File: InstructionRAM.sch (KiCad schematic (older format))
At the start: 6 parts, among them U18 IDT7008L15JG, U19 ATF22V10C-7PX, U20 IDT7008L15JG

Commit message: Use IDT 7024L15PFG dual port SRAM for the register file.
These are smaller and faster than the ICs I was using before, and I only
need two of them.
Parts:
- renumbered C23 to C69, C24 to C70, C25 to C71, U18 to U65, U19 to U66, U20 to U67

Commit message: Fix ERC errors and change operands in EX.
Now, A is the left operand and B is the right operand. The immediate
value may be selected for the right hand operand.
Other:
- note removed: "TODO: Consider replacing these two dual port SRAMs\nwith one 7028L20PFGI 64Kx16 dual port SRAM."
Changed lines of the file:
@@
 Wire Bus Line
 	6400 950  8650 950
-Text Notes 4300 1900 0    50   ~ 0
-TODO: Consider replacing these two dual port SRAMs\nwith one 7028L20PFGI 64Kx16 dual port SRAM.
 $Comp
 L power:GND #PWR?

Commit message: Add a "Mouser" field to components with a link to buy the part.
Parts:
- C68: renamed from C69; Mouser (none) -> https://www.mouser.com/ProductDetail/963-EMK107B7104KAHT
- C69: renamed from C70; Mouser (none) -> https://www.mouser.com/ProductDetail/963-EMK107B7104KAHT
- C70: renamed from C71; Mouser (none) -> https://www.mouser.com/ProductDetail/963-EMK107B7104KAHT
- U64: renamed from U65; Mouser (none) -> https://www.mouser.com/ProductDetail/Renesas-IDT/7008L15JG?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; Mouser2 (none) -> https://www.mouser.com/ProductDetail/3M-Electronic-Solution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
- U65: renamed from U66; Mouser (none) -> https://www.mouser.com/ProductDetail/Microchip-Technology-A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; Mouser2 (none) -> https://www.mouser.com/ProductDetail/575-4462401
- U66: renamed from U67; Mouser (none) -> https://www.mouser.com/ProductDetail/Renesas-IDT/7008L15JG?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; Mouser2 (none) -> https://www.mouser.com/ProductDetail/3M-Electronic-Solution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
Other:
- note added: "TODO: The ATF22V10 data sheet suggests connecting pin 15"

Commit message: The right operand can form an immediate value from several bit fields.
This solves the problem of the Store instruction not being able to compute
Ra+Imm as can be done in the Load instruction. Now, it can get those
immediate bits from the unused 'c' field.

Also, Jump isntructions which do not use the 'c' field to specify a link
register can use those bits to form an eight-bit immediate value.
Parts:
- renumbered C68 to C72, C69 to C73, C70 to C74, U64 to U68, U65 to U69, U66 to U70

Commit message: The Store Operand can take a byte-swapped value from the B register.
This enabled a version of the Store instruction which writes the upper
byte of the register to memory.
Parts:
- renumbered C72 to C74, C73 to C75, C74 to C76, U68 to U70, U69 to U71, U70 to U72

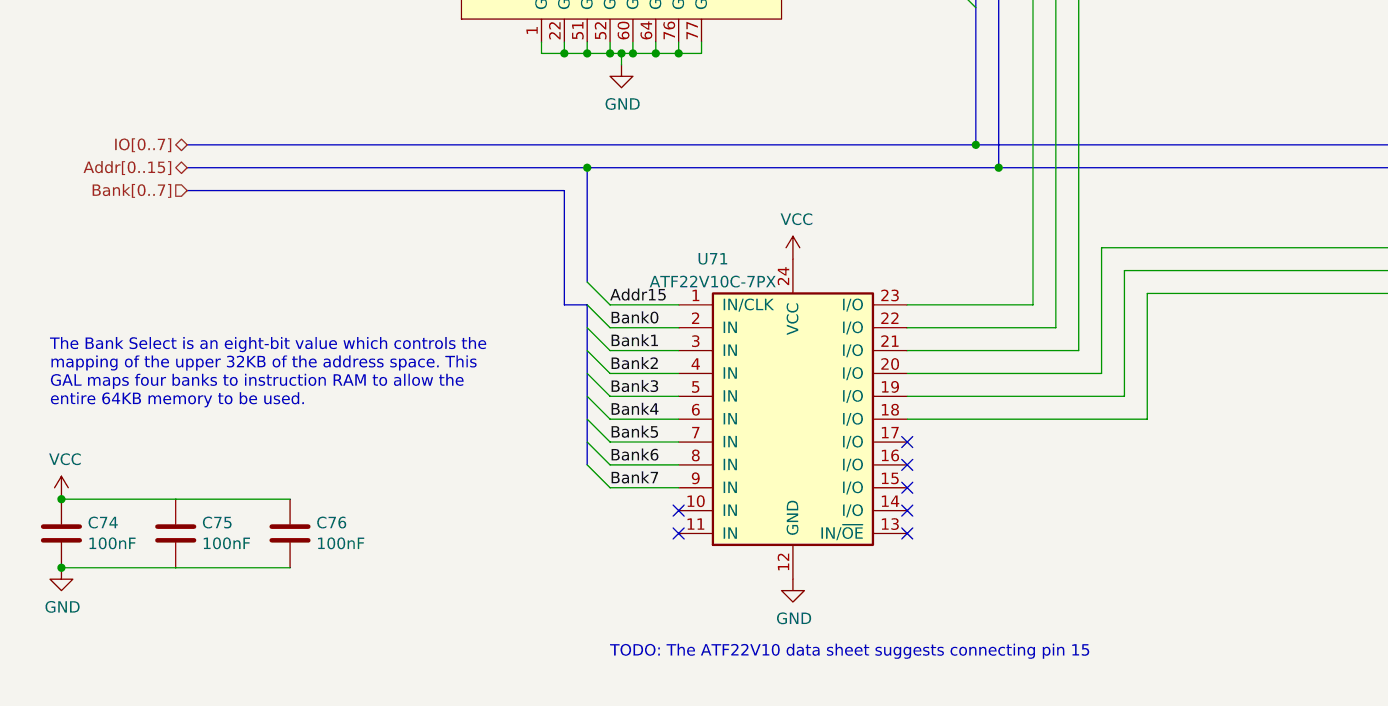
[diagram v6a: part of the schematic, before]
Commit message: Instruction RAM must accept MemLoad, MemStore, and Phi2 signals.
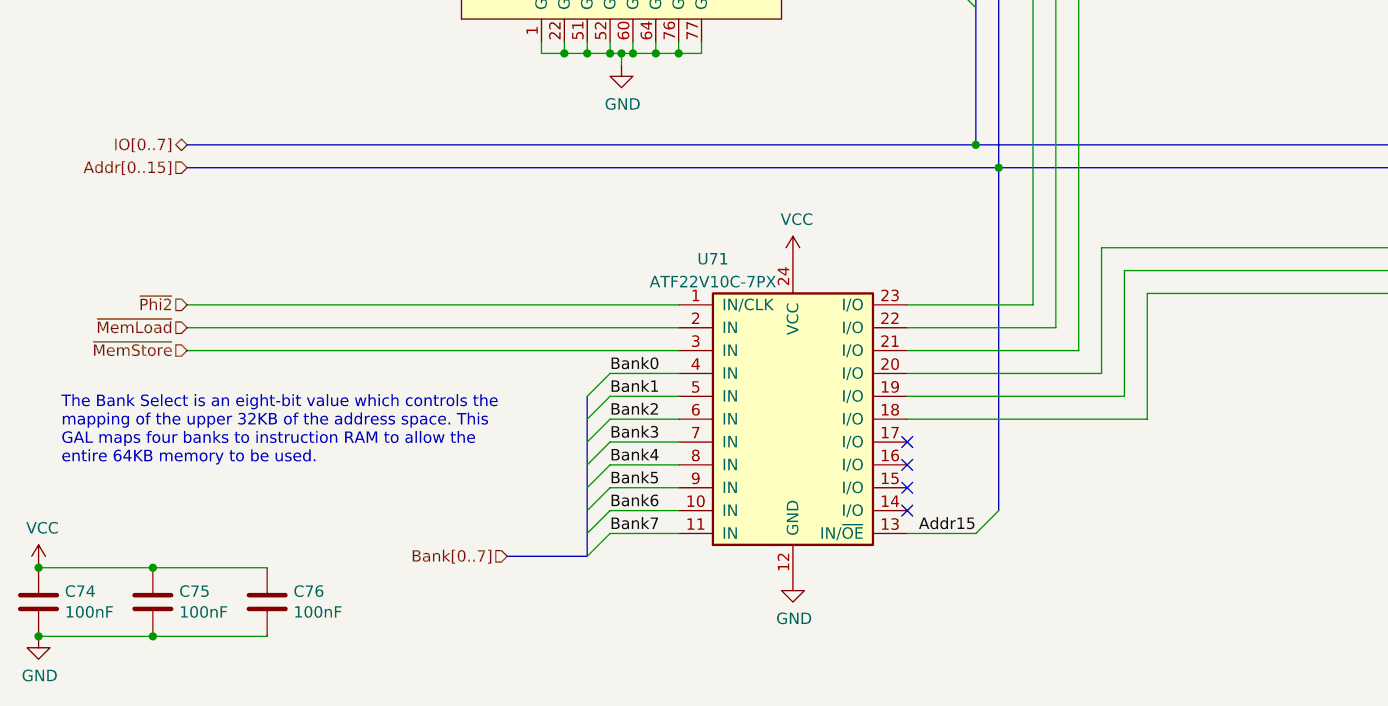
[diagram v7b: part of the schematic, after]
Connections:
- net Addr15: now also U71.13 (IN/~OE); no longer U71.1 (IN/CLK)
- net Bank0: now also U71.4 (IN); no longer U71.2 (IN)
- net Bank1: now also U71.5 (IN); no longer U71.3 (IN)
- net Bank2: now also U71.6 (IN); no longer U71.4 (IN)
- net Bank3: now also U71.7 (IN); no longer U71.5 (IN)
- net Bank4: now also U71.8 (IN); no longer U71.6 (IN)
- net Bank5: now also U71.9 (IN); no longer U71.7 (IN)
- net Bank6: now also U71.10 (IN); no longer U71.8 (IN)
- net Bank7: now also U71.11 (IN); no longer U71.9 (IN)
- new net ~MemLoad: U71.2 (IN)
- new net ~MemStore: U71.3 (IN)
- new net ~Phi2: U71.1 (IN/CLK)
- no-connect marks 11 -> 8
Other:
- note removed: "TODO: The ATF22V10 data sheet suggests connecting pin 15"
- moved on the sheet: C74, C75, C76
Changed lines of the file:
@@
 L Device:C C?
 U 1 1 5FD4710E
-P 700 7350
+P 600 7650
 AR Path="/5D8005AF/5D800742/5FD4710E" Ref="C?"  Part="1"
 AR Path="/5FE35007/5FD4710E" Ref="C?"  Part="1"
 AR Path="/5FE35007/5FD0D8DC/5FD4710E" Ref="C74"  Part="1"
-F 0 "C74" H 815 7396 50  0000 L CNN
-F 1 "100nF" H 815 7305 50  0000 L CNN
-F 2 "Capacitor_SMD:C_0603_1608Metric_Pad1.08x0.95mm_HandSolder" H 738 7200 50  0001 C CNN
-F 3 "~" H 700 7350 50  0001 C CNN
-F 4 "https://www.mouser.com/ProductDetail/963-EMK107B7104KAHT" H 700 7350 50  0001 C CNN "Mouser"
-	1    700  7350
+F 0 "C74" H 715 7696 50  0000 L CNN
+F 1 "100nF" H 715 7605 50  0000 L CNN
+F 2 "Capacitor_SMD:C_0603_1608Metric_Pad1.08x0.95mm_HandSolder" H 638 7500 50  0001 C CNN
+F 3 "~" H 600 7650 50  0001 C CNN
+F 4 "https://www.mouser.com/ProductDetail/963-EMK107B7104KAHT" H 600 7650 50  0001 C CNN "Mouser"
+	1    600  7650
 	1    0    0    -1
 $EndComp
@@
 L Device:C C?
 U 1 1 5FD47114
-P 1200 7350
+P 1100 7650
 AR Path="/5D8005AF/5D800742/5FD47114" Ref="C?"  Part="1"
 AR Path="/5FE35007/5FD47114" Ref="C?"  Part="1"
 AR Path="/5FE35007/5FD0D8DC/5FD47114" Ref="C75"  Part="1"
-F 0 "C75" H 1315 7396 50  0000 L CNN
-F 1 "100nF" H 1315 7305 50  0000 L CNN
-F 2 "Capacitor_SMD:C_0603_1608Metric_Pad1.08x0.95mm_HandSolder" H 1238 7200 50  0001 C CNN
-F 3 "~" H 1200 7350 50  0001 C CNN
-F 4 "https://www.mouser.com/ProductDetail/963-EMK107B7104KAHT" H 1200 7350 50  0001 C CNN "Mouser"
-	1    1200 7350
+F 0 "C75" H 1215 7696 50  0000 L CNN
+F 1 "100nF" H 1215 7605 50  0000 L CNN
+F 2 "Capacitor_SMD:C_0603_1608Metric_Pad1.08x0.95mm_HandSolder" H 1138 7500 50  0001 C CNN
+F 3 "~" H 1100 7650 50  0001 C CNN
+F 4 "https://www.mouser.com/ProductDetail/963-EMK107B7104KAHT" H 1100 7650 50  0001 C CNN "Mouser"
+	1    1100 7650
 	1    0    0    -1
 $EndComp
@@
 L power:GND #PWR?
 U 1 1 5FD4711A
-P 700 7500
+P 600 7800
 AR Path="/5D8005AF/5D800742/5FD4711A" Ref="#PWR?"  Part="1"
 AR Path="/5FE35007/5FD4711A" Ref="#PWR?"  Part="1"
 AR Path="/5FE35007/5FD0D8DC/5FD4711A" Ref="#PWR0450"  Part="1"
-F 0 "#PWR0450" H 700 7250 50  0001 C CNN
-F 1 "GND" H 705 7327 50  0000 C CNN
-F 2 "" H 700 7500 50  0001 C CNN
-F 3 "" H 700 7500 50  0001 C CNN
-	1    700  7500
+F 0 "#PWR0450" H 600 7550 50  0001 C CNN
+F 1 "GND" H 605 7627 50  0000 C CNN
+F 2 "" H 600 7800 50  0001 C CNN
+F 3 "" H 600 7800 50  0001 C CNN
+	1    600  7800
 	1    0    0    -1
 $EndComp
@@
 L power:VCC #PWR?
 U 1 1 5FD47120
-P 700 7200
+P 600 7500
 AR Path="/5D8005AF/5D800742/5FD47120" Ref="#PWR?"  Part="1"
 AR Path="/5FE35007/5FD47120" Ref="#PWR?"  Part="1"
 AR Path="/5FE35007/5FD0D8DC/5FD47120" Ref="#PWR0449"  Part="1"
-F 0 "#PWR0449" H 700 7050 50  0001 C CNN
-F 1 "VCC" H 717 7373 50  0000 C CNN
-F 2 "" H 700 7200 50  0001 C CNN
-F 3 "" H 700 7200 50  0001 C CNN
-	1    700  7200
+F 0 "#PWR0449" H 600 7350 50  0001 C CNN
+F 1 "VCC" H 617 7673 50  0000 C CNN
+F 2 "" H 600 7500 50  0001 C CNN
+F 3 "" H 600 7500 50  0001 C CNN
+	1    600  7500
 	1    0    0    -1
 $EndComp
 Wire Wire Line
-	700  7200 1200 7200
-Connection ~ 700  7200
-Wire Wire Line
-	1200 7500 700  7500
-Connection ~ 700  7500
+	600  7500 1100 7500
+Connection ~ 600  7500
+Wire Wire Line
+	1100 7800 600  7800
+Connection ~ 600  7800
 Entry Wire Line
 	6500 4250 6400 4150
@@
 L Device:C C?
 U 1 1 5FD472D1
-P 1700 7350
+P 1600 7650
 AR Path="/5D8005AF/5D800742/5FD472D1" Ref="C?"  Part="1"
 AR Path="/5FE35007/5FD472D1" Ref="C?"  Part="1"
 AR Path="/5FE35007/5FD0D8DC/5FD472D1" Ref="C76"  Part="1"
-F 0 "C76" H 1815 7396 50  0000 L CNN
-F 1 "100nF" H 1815 7305 50  0000 L CNN
-F 2 "Capacitor_SMD:C_0603_1608Metric_Pad1.08x0.95mm_HandSolder" H 1738 7200 50  0001 C CNN
-F 3 "~" H 1700 7350 50  0001 C CNN
-F 4 "https://www.mouser.com/ProductDetail/963-EMK107B7104KAHT" H 1700 7350 50  0001 C CNN "Mouser"
-	1    1700 7350
+F 0 "C76" H 1715 7696 50  0000 L CNN
+F 1 "100nF" H 1715 7605 50  0000 L CNN
+F 2 "Capacitor_SMD:C_0603_1608Metric_Pad1.08x0.95mm_HandSolder" H 1638 7500 50  0001 C CNN
+F 3 "~" H 1600 7650 50  0001 C CNN
+F 4 "https://www.mouser.com/ProductDetail/963-EMK107B7104KAHT" H 1600 7650 50  0001 C CNN "Mouser"
+	1    1600 7650
 	1    0    0    -1
 $EndComp
 Wire Wire Line
-	1200 7200 1700 7200
-Wire Wire Line
-	1700 7500 1200 7500
+	1100 7500 1600 7500
+Wire Wire Line
+	1600 7800 1100 7800
 Text HLabel 1250 5650 0    50   3State ~ 0
 IO[0..7]
-Text HLabel 1250 5750 0    50   3State ~ 0
+Text HLabel 1250 5750 0    50   Input ~ 0
 Addr[0..15]
 Wire Bus Line
@@
 Wire Wire Line
 	10150 2250 8950 2250
-Entry Wire Line
-	3000 6250 3100 6350
-Wire Wire Line
-	3100 6350 3400 6350
-Text Label 3100 6350 0    50   ~ 0
-Addr15
-Text HLabel 1250 5850 0    50   Input ~ 0
+Text HLabel 2650 7450 0    50   Input ~ 0
 Bank[0..7]
-Entry Wire Line
-	3000 6350 3100 6450
-Text Label 3100 6450 0    50   ~ 0
+Text Label 3100 6650 0    50   ~ 0
 Bank0
 Entry Wire Line
-	3000 6450 3100 6550
-Text Label 3100 6550 0    50   ~ 0
+	3100 6750 3000 6850
+Text Label 3100 6750 0    50   ~ 0
 Bank1
 Entry Wire Line
-	3000 6550 3100 6650
-Text Label 3100 6650 0    50   ~ 0
+	3100 6850 3000 6950
+Text Label 3100 6850 0    50   ~ 0
 Bank2
-Wire Bus Line
-	1250 5850 2900 5850
 Text Label 9700 3950 2    50   ~ 0
 Addr14
@@
 Entry Wire Line
 	4700 2550 4800 2650
-Text Notes 650  6800 0    50   ~ 0
+Text Notes 700  7050 0    50   ~ 0
 The Bank Select is an eight-bit value which controls the\nmapping of the upper 32KB of the address space. This\nGAL maps four banks to instruction RAM to allow the\nentire 64KB memory to be used.
-Wire Bus Line
-	1250 5750 3000 5750
-Connection ~ 3000 5750
-Wire Bus Line
-	3000 5750 4800 5750
 Wire Bus Line
 	4800 5750 9800 5750
 NoConn ~ 4400 6950
 NoConn ~ 4400 7050
-NoConn ~ 4400 7150
 NoConn ~ 4400 7250
-NoConn ~ 4400 7350
-NoConn ~ 3400 7250
-NoConn ~ 3400 7350
-Wire Bus Line
-	3000 5750 3000 6250
-Wire Wire Line
-	3100 6450 3400 6450
-Wire Wire Line
-	3100 6550 3400 6550
 Wire Wire Line
 	3100 6650 3400 6650
-Wire Bus Line
-	3000 6350 2900 6350
-Wire Bus Line
-	2900 6350 2900 5850
+Wire Wire Line
+	3100 6750 3400 6750
+Wire Wire Line
+	3100 6850 3400 6850
 $Comp
 L MainBoard-rescue:ATF22V10C-Logic_Programmable U?
@@
 $EndComp
 Entry Wire Line
-	3000 6650 3100 6750
-Text Label 3100 6750 0    50   ~ 0
+	3100 6950 3000 7050
+Text Label 3100 6950 0    50   ~ 0
 Bank3
 Entry Wire Line
-	3000 6750 3100 6850
-Text Label 3100 6850 0    50   ~ 0
+	3100 7050 3000 7150
+Text Label 3100 7050 0    50   ~ 0
 Bank4
 Entry Wire Line
-	3000 6850 3100 6950
-Text Label 3100 6950 0    50   ~ 0
+	3100 7150 3000 7250
+Text Label 3100 7150 0    50   ~ 0
 Bank5
 Wire Wire Line
-	3100 6750 3400 6750
-Wire Wire Line
-	3100 6850 3400 6850
-Wire Wire Line
 	3100 6950 3400 6950
-Entry Wire Line
-	3000 6950 3100 7050
-Text Label 3100 7050 0    50   ~ 0
+Wire Wire Line
+	3100 7050 3400 7050
+Wire Wire Line
+	3100 7150 3400 7150
+Entry Wire Line
+	3100 7250 3000 7350
+Text Label 3100 7250 0    50   ~ 0
 Bank6
 Entry Wire Line
-	3000 7050 3100 7150
-Text Label 3100 7150 0    50   ~ 0
+	3100 7350 3000 7450
+Text Label 3100 7350 0    50   ~ 0
 Bank7
 Wire Wire Line
-	3100 7050 3400 7050
-Wire Wire Line
-	3100 7150 3400 7150
+	3100 7250 3400 7250
+Wire Wire Line
+	3100 7350 3400 7350
 Wire Wire Line
 	4950 6350 4400 6350
@@
 NoConn ~ 2350 1850
 NoConn ~ 3950 1850
-Wire Bus Line
-	3000 6350 3000 7050
+Text HLabel 1250 6450 0    50   Input ~ 0
+~MemLoad
+Text HLabel 1250 6550 0    50   Input ~ 0
+~MemStore
+Text HLabel 1250 6350 0    50   Input ~ 0
+~Phi2
+Connection ~ 1100 7500
+Connection ~ 1100 7800
+Entry Wire Line
+	3100 6650 3000 6750
+Text Label 4700 7350 2    50   ~ 0
+Addr15
+Wire Wire Line
+	4700 7350 4400 7350
+Entry Wire Line
+	4800 7250 4700 7350
+Wire Bus Line
+	4800 5750 4800 7250
+Wire Bus Line
+	1250 5750 4800 5750
+Wire Bus Line
+	2650 7450 3000 7450
+Wire Wire Line
+	1250 6550 3400 6550
+Wire Wire Line
+	1250 6450 3400 6450
+Wire Wire Line
+	1250 6350 3400 6350
+NoConn ~ 4400 7150
+Wire Bus Line
+	3000 6750 3000 7450
 Wire Bus Line
 	9700 4350 9700 5650
@@
 Wire Bus Line
 	1500 650  1500 3950
-Text Notes 3100 7900 0    50   ~ 0
-TODO: The ATF22V10 data sheet suggests connecting pin 15
 $EndSCHEMATC
